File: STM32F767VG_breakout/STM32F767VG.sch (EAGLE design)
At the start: 36 parts, among them IC1 STM32F767VGT6, IC3 LD117AS33TR, X4 8MHz, X5 32.768kHz, X6 MSTBA2

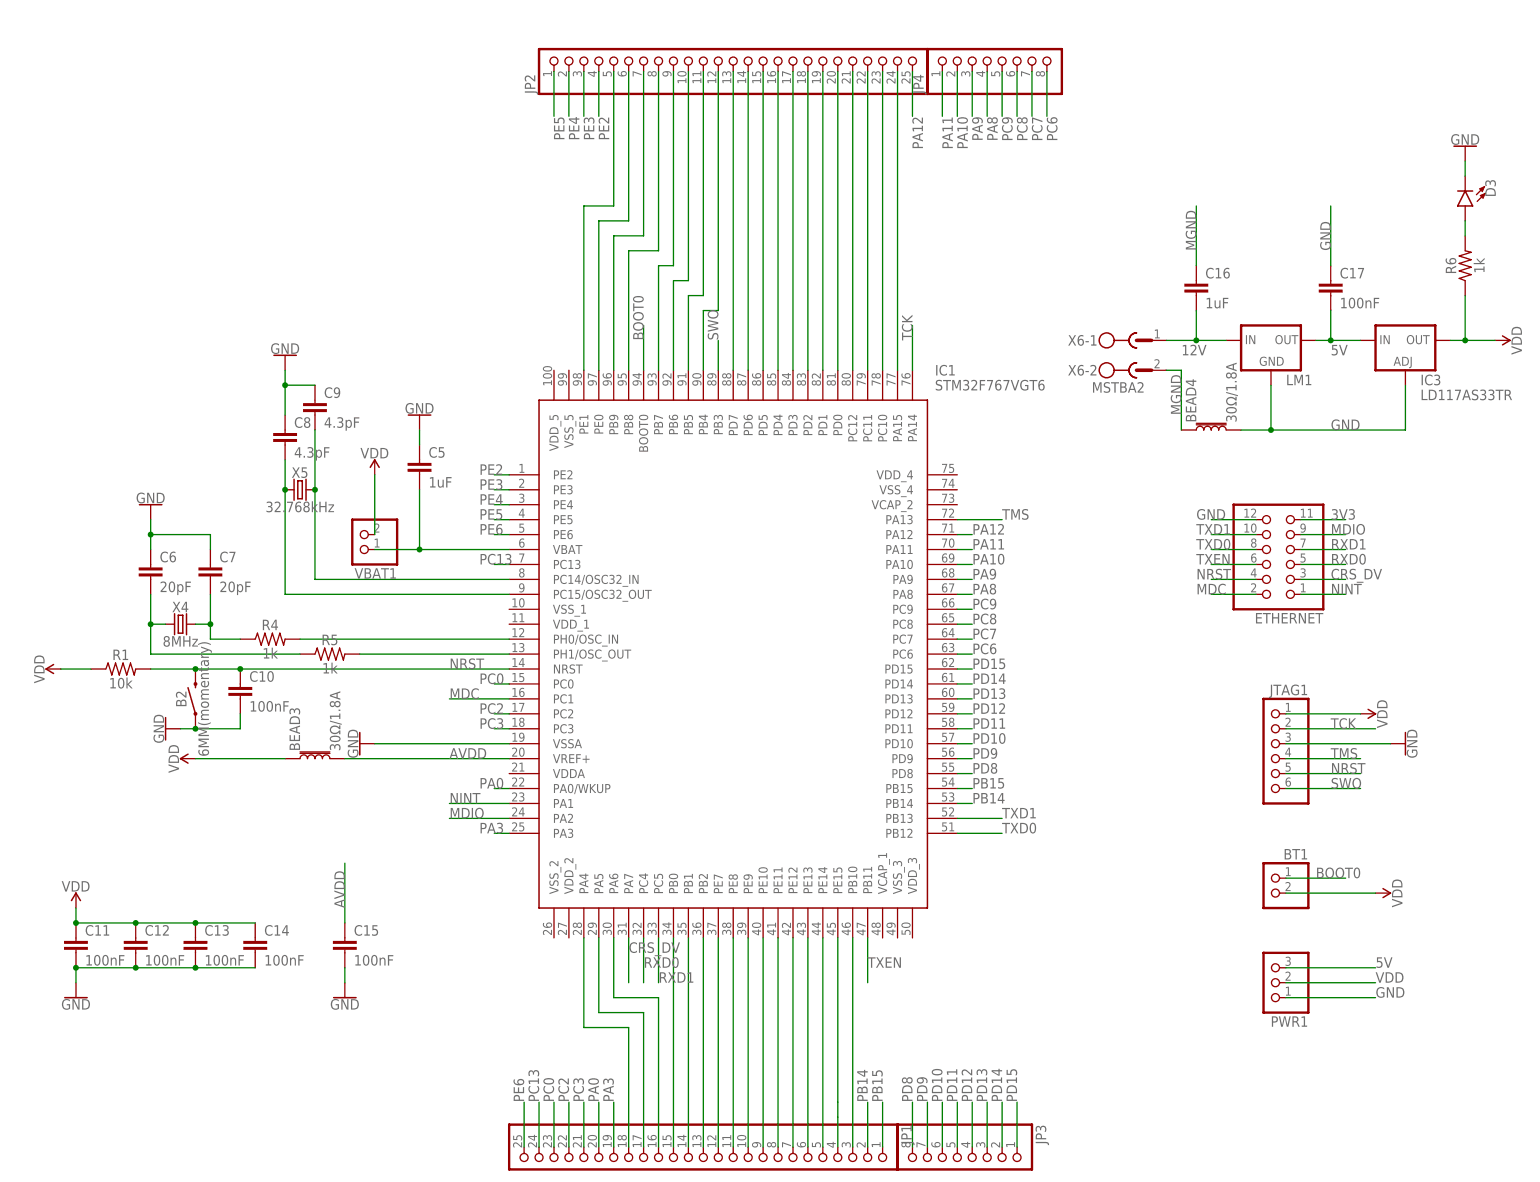
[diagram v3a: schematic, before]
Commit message: Incorporated small changes
As per February 9 2019 Slack message in the electrical channel.

1- connect the 3V3 of Ethernet breakout board to VDD
2- the 12v input should be provided in two ways: regular pin header / phoenix jack (already there)
3- Pull down the BOOT0 pin 10k ohm
4- Hook up LEDs to these pins on the microcontroller:
PD15(pin 62) - PD7(pin 88) - PD14(pin 61)

Still have to validate the crystal design
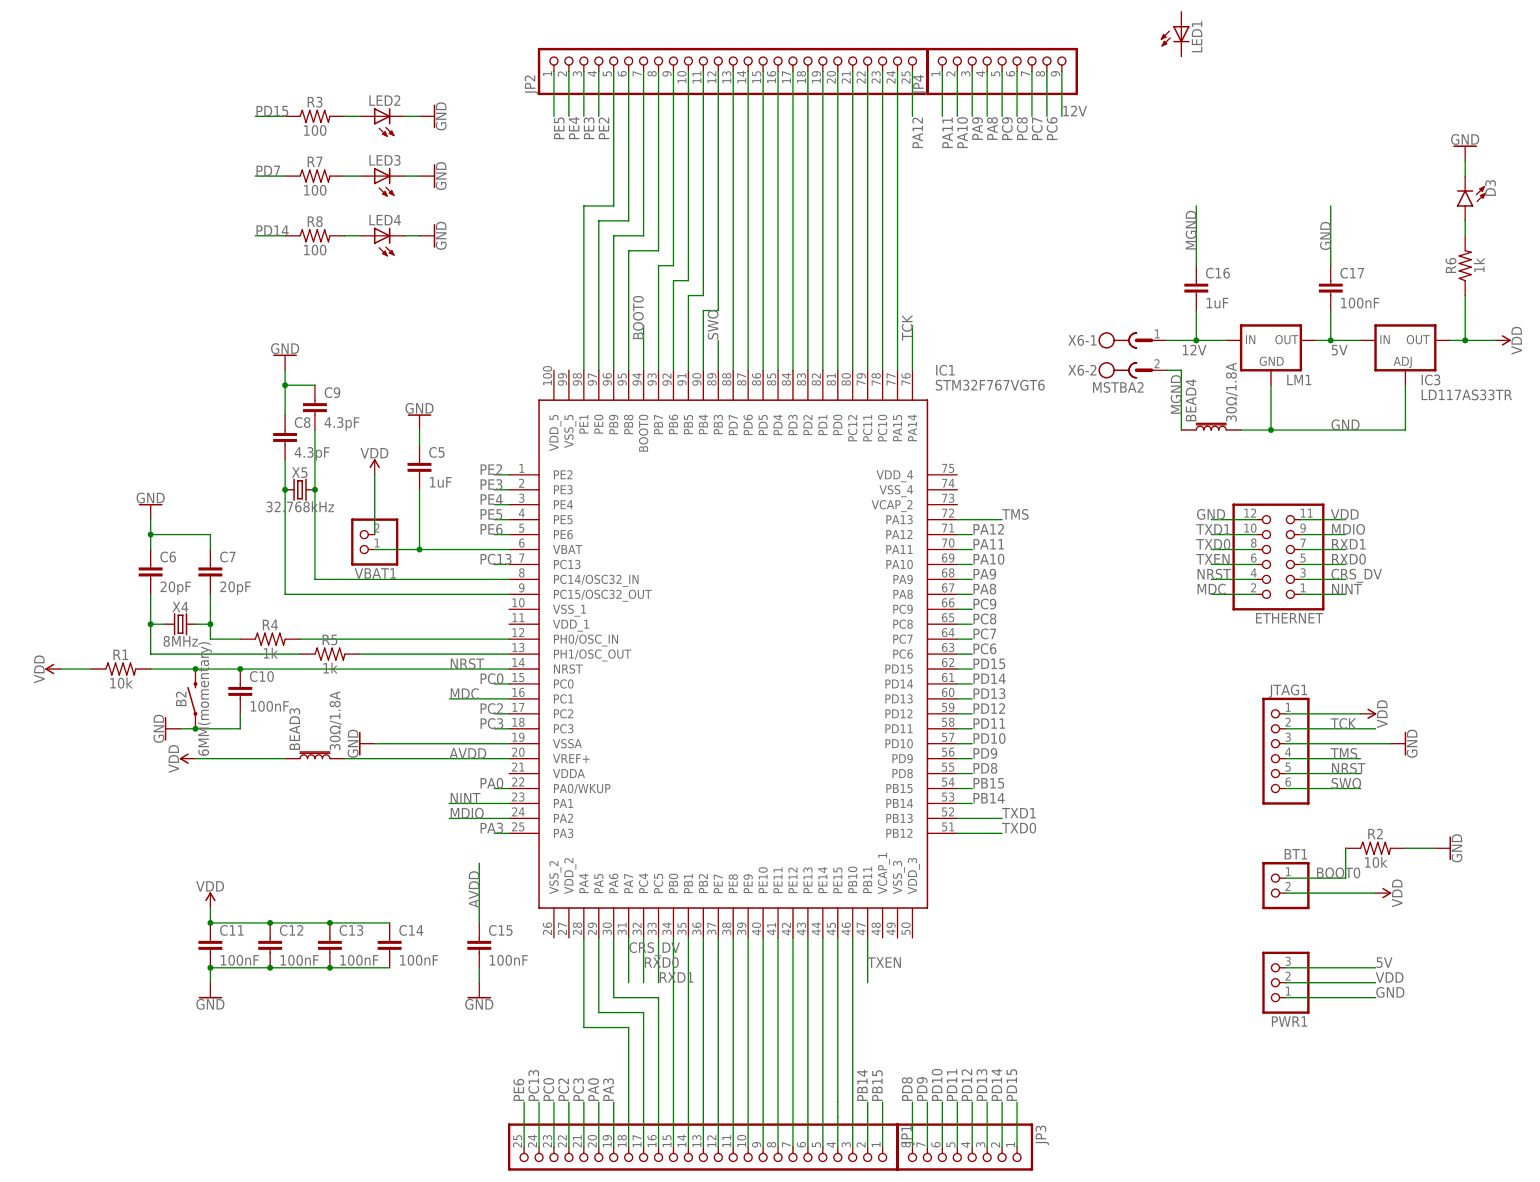
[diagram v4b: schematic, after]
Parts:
- added LED1, LED2, LED3, LED4: (no value), eagle-ltspice:LED_E
- added R2: 10k, SparkFun-Resistors:10KOHM-HORIZ-1/4W-1%
- added R3, R7, R8: 100, SparkFun-Resistors:10KOHM-HORIZ-1/4W-1%
- JP4: device pinhead:PINHD-1X8 -> pinhead:PINHD-1X9
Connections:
- removed net 3V3: ETHERNET.11
- new net N$17: LED2.A, R3.2
- new net N$26: LED3.A, R7.2
- new net N$27: LED4.A, R8.2
- new net PD7: R7.1
- net 12V: now also JP4.9
- net BOOT0: now also R2.1
- net GND: now also LED2.C, LED3.C, LED4.C, R2.2
- net PD14: now also R8.1
- net PD15: now also R3.1
- net VDD: now also ETHERNET.11
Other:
- moved on the sheet: C11, C12, C13, C14, C15

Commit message: Pre-design schematic done
Incorporated changes discussed in March 21 meeting
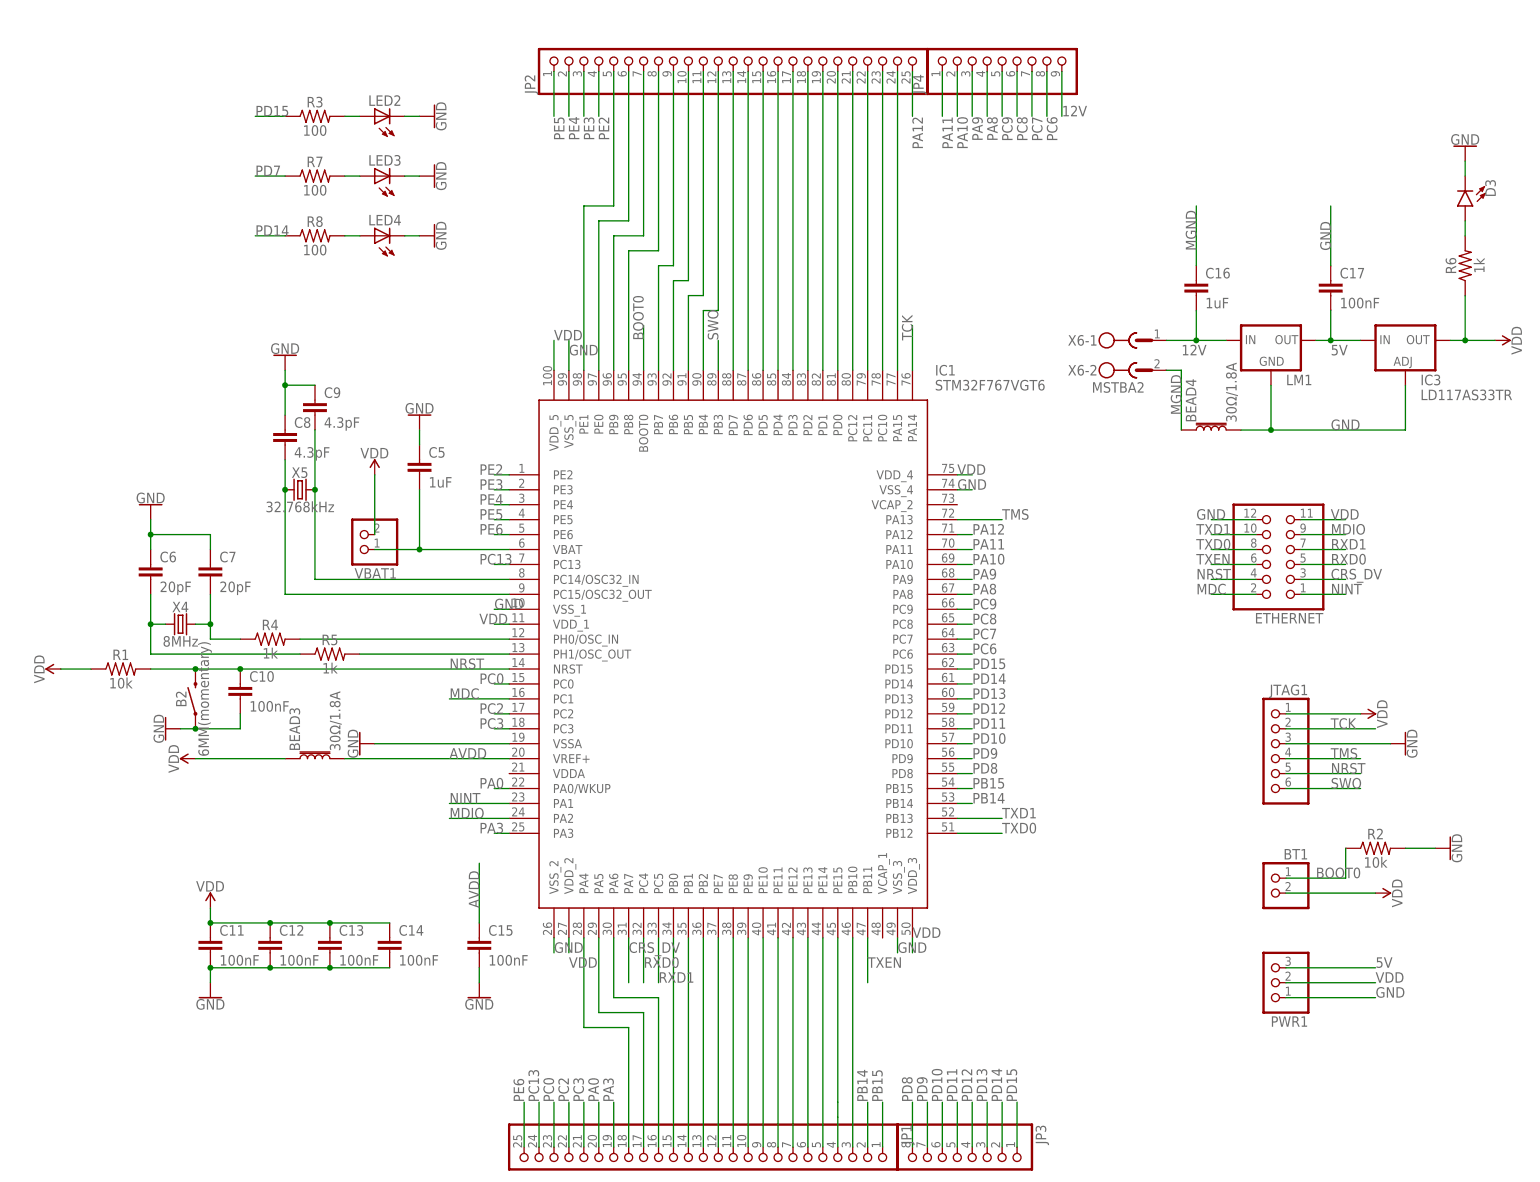
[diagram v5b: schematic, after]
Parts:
- removed LED1: (no value), eagle-ltspice:LED_E
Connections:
- net GND: now also IC1.VSS_1, IC1.VSS_2, IC1.VSS_3, IC1.VSS_4, IC1.VSS_5
- net VDD: now also IC1.VDD_1, IC1.VDD_2, IC1.VDD_3, IC1.VDD_4, IC1.VDD_5
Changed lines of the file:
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@@
 <part name="R2" library="SparkFun-Resistors" deviceset="10KOHM" device="-HORIZ-1/4W-1%" value="10k"/>
 <part name="GND1" library="SparkFun-PowerSymbols" deviceset="GND" device=""/>
-<part name="LED1" library="eagle-ltspice" library_urn="urn:adsk.eagle:library:217" deviceset="LED_E" device="" package3d_urn="urn:adsk.eagle:package:13319/1"/>
 <part name="LED2" library="eagle-ltspice" library_urn="urn:adsk.eagle:library:217" deviceset="LED_E" device="" package3d_urn="urn:adsk.eagle:package:13319/1"/>
 <part name="R3" library="SparkFun-Resistors" deviceset="10KOHM" device="-HORIZ-1/4W-1%" value="100"/>
@@
 <instance part="R2" gate="G$1" x="147.32" y="-63.5"/>
 <instance part="GND1" gate="1" x="160.02" y="-63.5" rot="R90"/>
-<instance part="LED1" gate="G$1" x="114.3" y="76.2"/>
 <instance part="LED2" gate="G$1" x="-22.86" y="60.96" rot="R90"/>
 <instance part="R3" gate="G$1" x="-33.02" y="60.96"/>
@@
 <wire x1="-15.24" y1="40.64" x2="-17.78" y2="40.64" width="0.1524" layer="91"/>
 </segment>
+<segment>
+<pinref part="IC1" gate="G$1" pin="VSS_1"/>
+<wire x1="0" y1="-22.86" x2="-2.54" y2="-22.86" width="0.1524" layer="91"/>
+<label x="-2.54" y="-22.86" size="1.778" layer="95"/>
+</segment>
+<segment>
+<pinref part="IC1" gate="G$1" pin="VSS_3"/>
+<wire x1="66.04" y1="-78.74" x2="66.04" y2="-81.28" width="0.1524" layer="91"/>
+<label x="66.04" y="-81.28" size="1.778" layer="95"/>
+</segment>
+<segment>
+<pinref part="IC1" gate="G$1" pin="VSS_2"/>
+<wire x1="7.62" y1="-78.74" x2="7.62" y2="-81.28" width="0.1524" layer="91"/>
+<label x="7.62" y="-81.28" size="1.778" layer="95"/>
+</segment>
+<segment>
+<pinref part="IC1" gate="G$1" pin="VSS_4"/>
+<wire x1="76.2" y1="-2.54" x2="78.74" y2="-2.54" width="0.1524" layer="91"/>
+<label x="76.2" y="-2.54" size="1.778" layer="95"/>
+</segment>
+<segment>
+<pinref part="IC1" gate="G$1" pin="VSS_5"/>
+<wire x1="10.16" y1="17.78" x2="10.16" y2="22.86" width="0.1524" layer="91"/>
+<label x="10.16" y="20.32" size="1.778" layer="95"/>
+</segment>
 </net>
 <net name="VDD" class="0">
@@
 <label x="139.7" y="-7.62" size="1.778" layer="95"/>
 </segment>
+<segment>
+<pinref part="IC1" gate="G$1" pin="VDD_1"/>
+<wire x1="0" y1="-25.4" x2="-2.54" y2="-25.4" width="0.1524" layer="91"/>
+<label x="-5.08" y="-25.4" size="1.778" layer="95"/>
+</segment>
+<segment>
+<pinref part="IC1" gate="G$1" pin="VDD_3"/>
+<wire x1="68.58" y1="-78.74" x2="68.58" y2="-81.28" width="0.1524" layer="91"/>
+<label x="68.58" y="-78.74" size="1.778" layer="95"/>
+</segment>
+<segment>
+<pinref part="IC1" gate="G$1" pin="VDD_2"/>
+<wire x1="10.16" y1="-78.74" x2="10.16" y2="-81.28" width="0.1524" layer="91"/>
+<label x="10.16" y="-83.82" size="1.778" layer="95"/>
+</segment>
+<segment>
+<pinref part="IC1" gate="G$1" pin="VDD_4"/>
+<wire x1="76.2" y1="0" x2="78.74" y2="0" width="0.1524" layer="91"/>
+<label x="76.2" y="0" size="1.778" layer="95"/>
+</segment>
+<segment>
+<pinref part="IC1" gate="G$1" pin="VDD_5"/>
+<wire x1="7.62" y1="17.78" x2="7.62" y2="22.86" width="0.1524" layer="91"/>
+<label x="7.62" y="22.86" size="1.778" layer="95"/>
+</segment>
 </net>
